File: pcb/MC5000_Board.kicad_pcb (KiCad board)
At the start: 2 copper layers, 100 x 97.5 mm, 44 parts, among them J1 USB_B_Micro, J10 Conn_01x04_Male, J11 Conn_01x04_Male, J12 Conn_01x04_Male, J13 Conn_01x04_Male, J2 Conn_01x04_Male, J3 Conn_01x04_Male, J4 Conn_01x04_Male, J5 Conn_01x04_Male, J6 Conn_01x04_Male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

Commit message: fixes
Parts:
- added C3: 0.1uF, Capacitor_SMD:C_0603_1608Metric_Pad1.08x0.95mm_HandSolder, F.Cu at (106.0, 46.5)
- added C4: 0.1uF, Capacitor_SMD:C_0603_1608Metric_Pad1.08x0.95mm_HandSolder, F.Cu at (110.5, 57.2)
- added D1: LED, LED_SMD:LED_0805_2012Metric_Pad1.15x1.40mm_HandSolder, F.Cu at (53.9, 54.8)
- added J14: Conn_01x04_Female, Connector_PinSocket_2.54mm:PinSocket_1x04_P2.54mm_Vertical, F.Cu at (106.7, 57.2)
- added J15: Conn_01x04_Female, Connector_PinSocket_2.54mm:PinSocket_1x04_P2.54mm_Vertical, F.Cu at (114.3, 64.8)
- added R10: 10k, Resistor_SMD:R_0603_1608Metric_Pad0.98x0.95mm_HandSolder, F.Cu at (110.5, 65.3)
- added R11: 10k, Resistor_SMD:R_0603_1608Metric_Pad0.98x0.95mm_HandSolder, F.Cu at (110.5, 62.6)
- added R12: 10k, Resistor_SMD:R_0603_1608Metric_Pad0.98x0.95mm_HandSolder, F.Cu at (110.5, 59.9)
- added R9: 200R, Resistor_SMD:R_0603_1608Metric_Pad0.98x0.95mm_HandSolder, F.Cu at (54.1, 44.4)
- moved U8 2.70 mm to (112.3, 48.5)
- moved DS1 2.48 mm to (76.1, 54.5)
- moved R1 2.48 mm to (100.2, 44.5)
- moved R2 2.48 mm to (100.2, 61.4)
- moved R3 2.48 mm to (100.2, 58.7)
- moved R4 2.48 mm to (100.2, 55.9)
- moved R5 2.48 mm to (100.2, 50.0)
- moved R6 2.48 mm to (100.2, 47.4)
- moved R7 2.48 mm to (100.2, 53.1)
- moved R8 2.48 mm to (100.2, 64.5)
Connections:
- U8 pad 12: Net-(U8-Pad12) -> GND
- U8 pad 2: Net-(U8-Pad2) -> GND
- U8 pad 21: Net-(U8-Pad21) -> GND
- U8 pad 24: Net-(U8-Pad24) -> VCC
- U8 pad 3: Net-(U8-Pad3) -> GND
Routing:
- net VCC: track 10.1 -> 146.4 mm, vias 2 -> 3
- net Net-(R9-Pad2): track 0.00 -> 70.4 mm
- net Net-(J15-Pad1): track 0.00 -> 29.7 mm
- net Net-(J15-Pad2): track 0.00 -> 26.9 mm
- net Net-(R8-Pad2): track 0.00 -> 22.8 mm
- net Net-(R2-Pad2): track 0.00 -> 19.7 mm
- net Net-(R5-Pad2): track 0.00 -> 19.0 mm
- net Net-(R1-Pad2): track 0.00 -> 18.0 mm
- net Net-(J15-Pad3): track 0.00 -> 17.8 mm, vias 0 -> 1
- net Net-(R3-Pad2): track 0.00 -> 16.7 mm
- net Net-(R4-Pad2): track 0.00 -> 14.8 mm
- net Net-(DS1-Pad8): track 25.3 -> 39.2 mm
- net Net-(DS1-Pad12): track 36.9 -> 50.8 mm
- net Net-(R6-Pad2): track 0.00 -> 13.4 mm
- net Net-(DS1-Pad7): track 21.0 -> 34.4 mm
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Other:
- board text added: "Buzzer IC"

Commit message: Work on PCB
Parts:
- added C5: 0.1uF, Capacitor_SMD:C_0603_1608Metric_Pad1.08x0.95mm_HandSolder, F.Cu at (61.5, 87.7)
- added C6: C, Capacitor_SMD:C_0603_1608Metric_Pad1.08x0.95mm_HandSolder, F.Cu at (69.3, 88.6)
- added C7: C, Capacitor_SMD:C_0603_1608Metric_Pad1.08x0.95mm_HandSolder, F.Cu at (69.3, 97.5)
- added J16: Conn_01x04_Female, Connector_PinSocket_2.54mm:PinSocket_1x04_P2.54mm_Vertical, F.Cu at (57.6, 87.8)
- added J17: Conn_01x04_Female, Connector_PinSocket_2.54mm:PinSocket_1x04_P2.54mm_Vertical, F.Cu at (57.9, 79.7)
- added J18: Conn_01x04_Female, Connector_PinSocket_2.54mm:PinSocket_1x04_P2.54mm_Vertical, F.Cu at (65.3, 95.4)
- added R13: 1M, Resistor_SMD:R_0603_1608Metric_Pad0.98x0.95mm_HandSolder, F.Cu at (61.5, 93.5)
- added R14: 1M, Resistor_SMD:R_0603_1608Metric_Pad0.98x0.95mm_HandSolder, F.Cu at (61.5, 90.6)
- added R15: 1M, Resistor_SMD:R_0603_1608Metric_Pad0.98x0.95mm_HandSolder, F.Cu at (69.3, 91.6)
- added R16: 1M, Resistor_SMD:R_0603_1608Metric_Pad0.98x0.95mm_HandSolder, F.Cu at (69.3, 94.5)
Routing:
- net Net-(J16-Pad3): track 0.00 -> 20.8 mm
- net Net-(C7-Pad2): track 0.00 -> 20.7 mm
- net Net-(J16-Pad2): track 0.00 -> 18.2 mm
- net TXD: track 10.6 -> 28.3 mm, vias 2 -> 1
- net Net-(C6-Pad2): track 0.00 -> 14.9 mm
- net VCC: track 146.4 -> 154.1 mm
- net RXD: track 14.4 -> 21.1 mm
- net Net-(J18-Pad2): track 0.00 -> 3.61 mm
- net Net-(J18-Pad1): track 0.00 -> 3.46 mm

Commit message: Nice labels
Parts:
- added ?: , buzzard_labels, F.Cu at (110.2, 66.5)
- added ?: , buzzard_labels, F.Cu at (61.9, 99.2)
- added ?: , buzzard_labels, F.Cu at (60.4, 105.5)
- added ?: , buzzard_labels, F.Cu at (65.7, 76.3)
- added ?: , buzzard_labels, F.Cu at (63.1, 76.5)
- added ?: , buzzard_labels, F.Cu at (60.5, 76.3)
- added ?: , buzzard_labels, F.Cu at (57.9, 76.5)
- added ?: , buzzard_labels, F.Cu at (61.8, 71.5)
- added ?: , buzzard_labels, F.Cu at (75.9, 67.1)
- added ?: , buzzard_labels, F.Cu at (140.0, 136.1)
- added ?: , buzzard_labels, F.Cu at (108.0, 136.1)
- added ?: , buzzard_labels, F.Cu at (124.0, 136.1)
- added ?: , buzzard_labels, F.Cu at (92.0, 136.1)
- added ?: , buzzard_labels, F.Cu at (75.8, 136.1)
- added ?: , buzzard_labels, F.Cu at (60.1, 136.1)
- R15, R16: value 1M -> 2K2
- moved C6 1.50 mm to (69.3, 87.1)
- moved C7 1.50 mm to (69.3, 96.0)
- moved R15 1.50 mm to (69.3, 90.1)
- moved R16 1.50 mm to (69.3, 93.0)
- moved J16 1.10 mm to (57.6, 88.9)
- moved R10 1.10 mm to (110.5, 64.2)
- moved R14 1.10 mm to (61.5, 91.7)
- moved C3 1.10 mm to (106.0, 45.4)
- moved C4 1.10 mm to (110.5, 56.1)
- moved DS1 1.10 mm to (76.1, 53.4)
- moved J14 1.10 mm to (106.7, 56.1)
- moved J15 1.10 mm to (114.3, 63.7)
- moved R1 1.10 mm to (100.2, 43.4)
- moved R11 1.10 mm to (110.5, 61.5)
- moved R12 1.10 mm to (110.5, 58.8)
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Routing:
- net Net-(J12-Pad1): track 16.9 -> 11.8 mm
- net Net-(C7-Pad2): track 20.7 -> 18.0 mm
- net Net-(C6-Pad2): track 14.9 -> 13.2 mm
- net Net-(J18-Pad2): track 3.61 -> 5.14 mm
- net Net-(J18-Pad1): track 3.46 -> 4.90 mm
- net VCC: track 154.1 -> 155.3 mm
- net RXD: track 21.1 -> 19.9 mm
- net TXD: track 28.3 -> 27.2 mm
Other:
- board text removed: "Buzzer IC"
- board text removed: "Display IC"
- board text removed: "MCU #1"
- board text removed: "MCU #2"
- board text removed: "MCU #3"

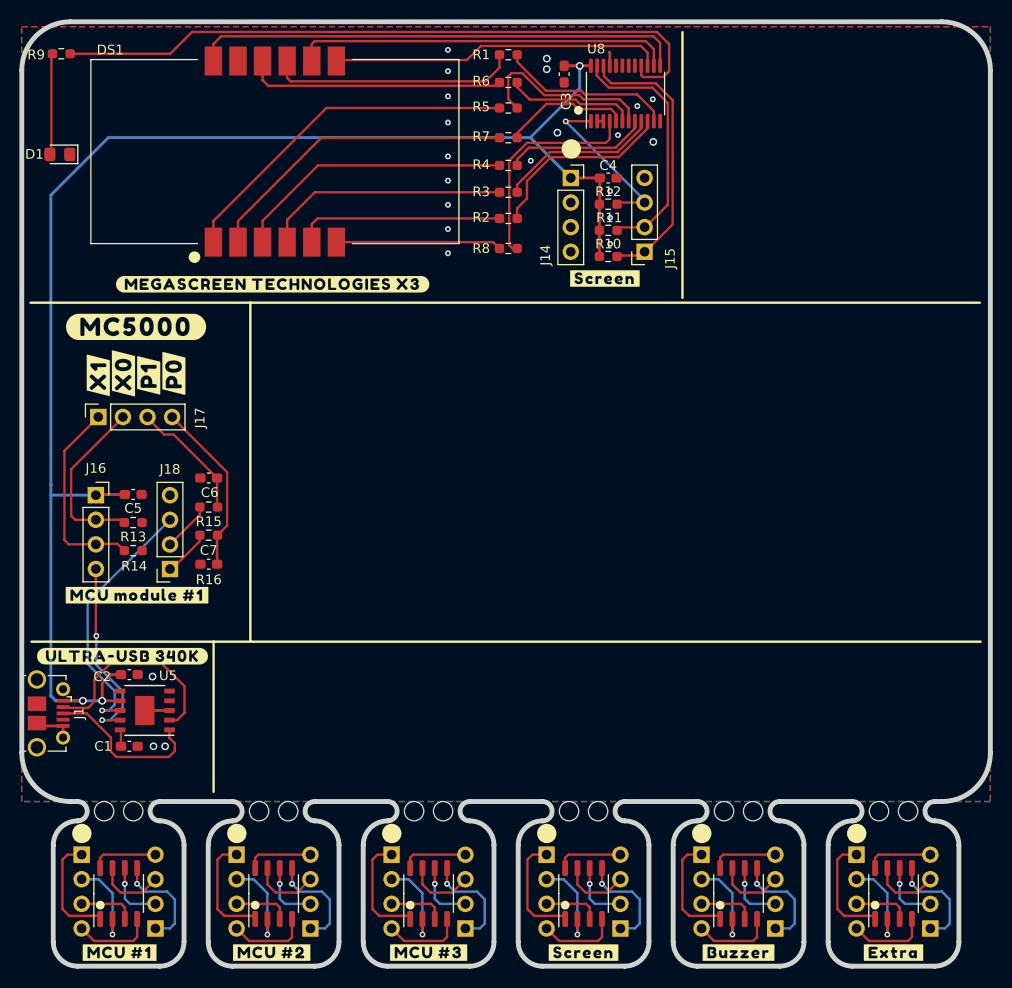
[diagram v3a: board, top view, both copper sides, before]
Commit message: Added buzzer
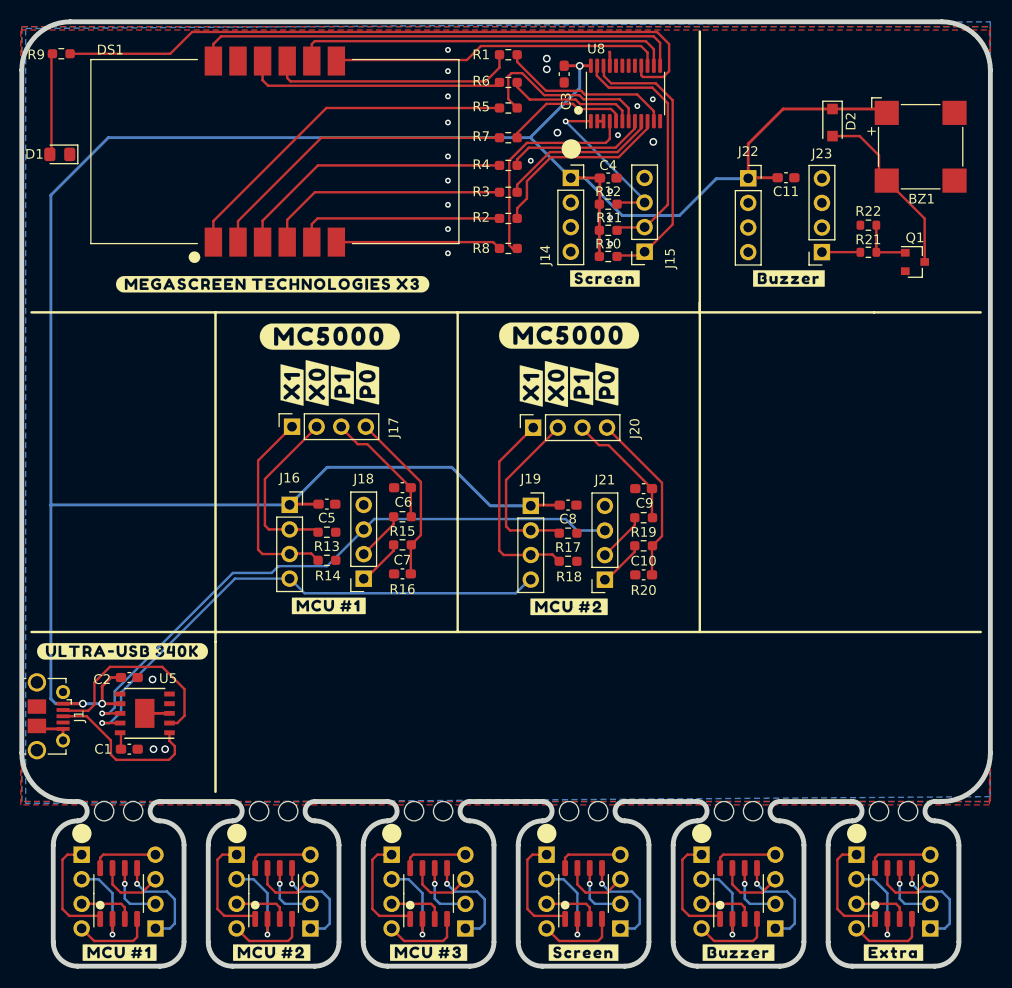
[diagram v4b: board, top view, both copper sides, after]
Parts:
- removed the ? at (61.9, 99.2)
- removed the ? at (65.7, 76.3)
- removed the ? at (63.1, 76.5)
- removed the ? at (60.5, 76.3)
- removed the ? at (57.9, 76.5)
- removed the ? at (61.8, 71.5)
- added ?: , buzzard_labels, F.Cu at (129.2, 66.5)
- added ?: , buzzard_labels, F.Cu at (81.8, 72.5)
- added ?: , buzzard_labels, F.Cu at (85.7, 77.3)
- added ?: , buzzard_labels, F.Cu at (106.5, 100.4)
- added ?: , buzzard_labels, F.Cu at (83.1, 77.5)
- added ?: , buzzard_labels, F.Cu at (80.5, 77.3)
- added ?: , buzzard_labels, F.Cu at (77.9, 77.5)
- added ?: , buzzard_labels, F.Cu at (81.7, 100.3)
- added ?: , buzzard_labels, F.Cu at (110.4, 77.4)
- added ?: , buzzard_labels, F.Cu at (105.2, 77.4)
- added ?: , buzzard_labels, F.Cu at (102.6, 77.6)
- added ?: , buzzard_labels, F.Cu at (107.8, 77.6)
- added ?: , buzzard_labels, F.Cu at (106.5, 72.4)
- added BZ1: MLT-7525, Buzzer_Beeper:MagneticBuzzer_CUI_CMT-8504-100-SMT, F.Cu at (142.8, 52.9)
- added C10: C, Capacitor_SMD:C_0603_1608Metric_Pad1.08x0.95mm_HandSolder, F.Cu at (114.2, 97.1)
- added C11: 0.1uF, Capacitor_SMD:C_0603_1608Metric_Pad1.08x0.95mm_HandSolder, F.Cu at (128.9, 56.1)
- added C8: 0.1uF, Capacitor_SMD:C_0603_1608Metric_Pad1.08x0.95mm_HandSolder, F.Cu at (106.4, 89.9)
- added C9: C, Capacitor_SMD:C_0603_1608Metric_Pad1.08x0.95mm_HandSolder, F.Cu at (114.2, 88.2)
- added D2: D, Diode_SMD:D_SOD-123F, F.Cu at (133.7, 50.4)
- added J19: Conn_01x04_Female, Connector_PinSocket_2.54mm:PinSocket_1x04_P2.54mm_Vertical, F.Cu at (102.5, 90.0)
- added J20: Conn_01x04_Female, Connector_PinSocket_2.54mm:PinSocket_1x04_P2.54mm_Vertical, F.Cu at (102.8, 81.9)
- added J21: Conn_01x04_Female, Connector_PinSocket_2.54mm:PinSocket_1x04_P2.54mm_Vertical, F.Cu at (110.2, 97.6)
- added J22: Conn_01x04_Female, Connector_PinSocket_2.54mm:PinSocket_1x04_P2.54mm_Vertical, F.Cu at (125.0, 56.2)
- added J23: Conn_01x04_Female, Connector_PinSocket_2.54mm:PinSocket_1x04_P2.54mm_Vertical, F.Cu at (132.6, 63.8)
- added Q1: S9013, Package_TO_SOT_SMD:SOT-23, F.Cu at (142.2, 64.8)
- added R17: 1M, Resistor_SMD:R_0603_1608Metric_Pad0.98x0.95mm_HandSolder, F.Cu at (106.4, 95.7)
- added R18: 1M, Resistor_SMD:R_0603_1608Metric_Pad0.98x0.95mm_HandSolder, F.Cu at (106.4, 92.8)
- added R19: 2K2, Resistor_SMD:R_0603_1608Metric_Pad0.98x0.95mm_HandSolder, F.Cu at (114.2, 91.2)
- added R20: 2K2, Resistor_SMD:R_0603_1608Metric_Pad0.98x0.95mm_HandSolder, F.Cu at (114.2, 94.1)
- added R21: 100R, Resistor_SMD:R_0603_1608Metric, F.Cu at (137.4, 63.8)
- added R22: 100k, Resistor_SMD:R_0603_1608Metric, F.Cu at (137.4, 61.0)
- moved J16 20.0 mm to (77.7, 89.9)
- moved J17 20.0 mm to (77.9, 81.8)
- moved C5 20.0 mm to (81.5, 89.8)
- moved C6 20.0 mm to (89.3, 88.1)
- moved C7 20.0 mm to (89.3, 97.0)
- moved J18 20.0 mm to (85.3, 97.5)
- moved R13 20.0 mm to (81.5, 95.6)
- moved R14 20.0 mm to (81.5, 92.7)
- moved R15 20.0 mm to (89.3, 91.1)
- moved R16 20.0 mm to (89.3, 94.0)
- moved ? 0.50 mm to (60.4, 105.0)
- moved U5 0.30 mm to (62.7, 111.4)
- moved C1 0.30 mm to (61.1, 115.1)
- moved C2 0.30 mm to (61.1, 107.7)
- moved J1 0.30 mm to (52.8, 111.7)
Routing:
- net VCC: track 155.3 -> 251.7 mm
- net TXD: track 27.2 -> 63.5 mm
- net RXD: track 19.9 -> 54.7 mm, vias 2 -> 1
- net Net-(J19-Pad3): track 0.00 -> 20.8 mm
- net Net-(BZ1-Pad2): track 0.00 -> 18.6 mm
- net Net-(J19-Pad2): track 0.00 -> 18.2 mm
- net Net-(C10-Pad2): track 0.00 -> 18.0 mm
- net Net-(C9-Pad2): track 0.00 -> 13.2 mm
- net Net-(Q1-Pad1): track 0.00 -> 5.81 mm
- net Net-(J21-Pad2): track 0.00 -> 5.14 mm
- net Net-(J21-Pad1): track 0.00 -> 4.90 mm
- net Net-(J23-Pad1): track 0.00 -> 3.97 mm

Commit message: Added LEDs
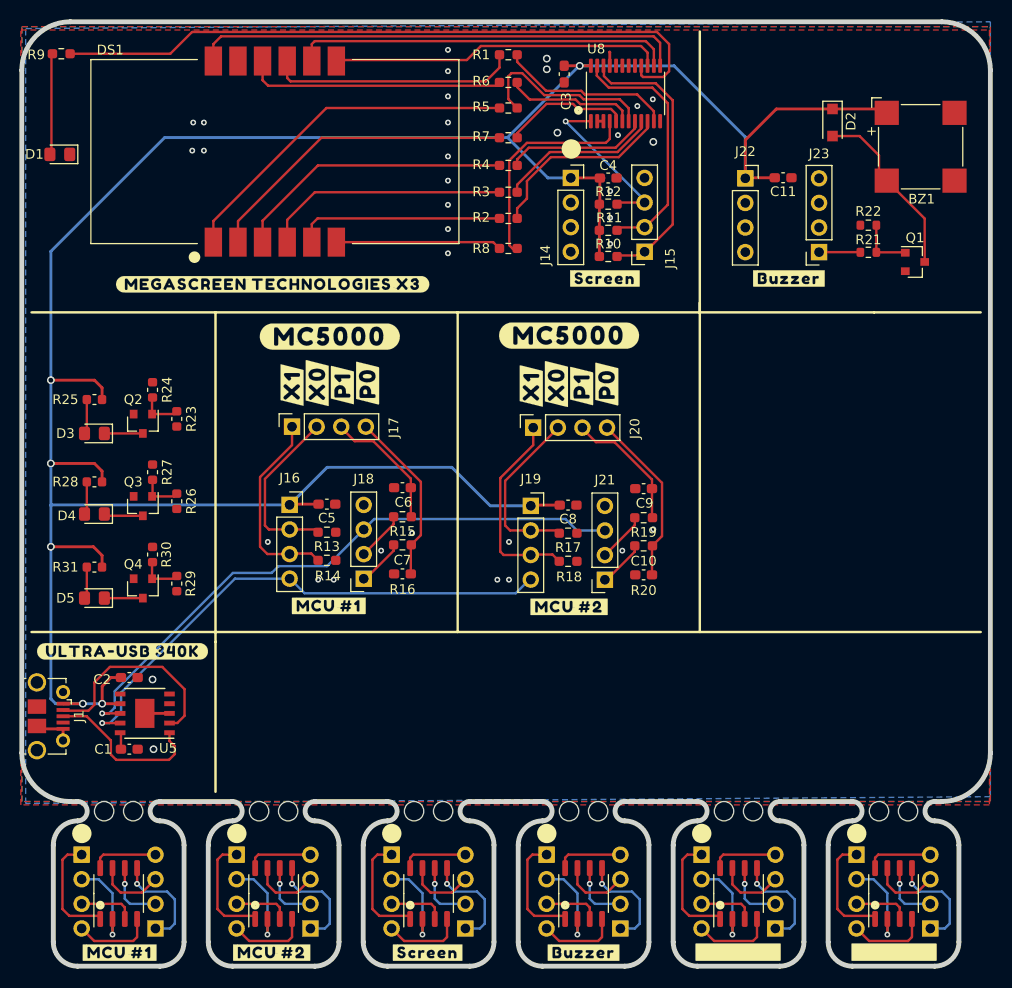
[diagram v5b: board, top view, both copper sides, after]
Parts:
- removed the ? at (140.0, 136.1)
- removed the ? at (92.0, 136.1)
- added D3: LED, LED_SMD:LED_0805_2012Metric_Pad1.15x1.40mm_HandSolder, F.Cu at (57.5, 82.5)
- added D4: LED, LED_SMD:LED_0805_2012Metric_Pad1.15x1.40mm_HandSolder, F.Cu at (57.5, 90.8)
- added D5: LED, LED_SMD:LED_0805_2012Metric_Pad1.15x1.40mm_HandSolder, F.Cu at (57.5, 99.5)
- added Q2: S9013, Package_TO_SOT_SMD:SOT-23, F.Cu at (62.5, 81.5)
- added Q3: S9013, Package_TO_SOT_SMD:SOT-23, F.Cu at (62.5, 90.0)
- added Q4: S9013, Package_TO_SOT_SMD:SOT-23, F.Cu at (62.5, 98.5)
- added R23: 100R, Resistor_SMD:R_0603_1608Metric, F.Cu at (66.0, 81.0)
- added R24: 100k, Resistor_SMD:R_0603_1608Metric, F.Cu at (63.5, 78.0)
- added R25: 150R, Resistor_SMD:R_0603_1608Metric, F.Cu at (57.5, 79.0)
- added R26: 100R, Resistor_SMD:R_0603_1608Metric, F.Cu at (66.0, 89.5)
- added R27: 100k, Resistor_SMD:R_0603_1608Metric, F.Cu at (63.5, 86.5)
- added R28: 150R, Resistor_SMD:R_0603_1608Metric, F.Cu at (57.5, 87.5)
- added R29: 100R, Resistor_SMD:R_0603_1608Metric, F.Cu at (66.0, 98.0)
- added R30: 100k, Resistor_SMD:R_0603_1608Metric, F.Cu at (63.5, 95.0)
- added R31: 150R, Resistor_SMD:R_0603_1608Metric, F.Cu at (57.5, 96.3)
- moved ? 16.1 mm to (91.9, 136.1)
- moved ? 16.0 mm to (108.0, 136.1)
- moved C11 0.30 mm to (128.6, 56.1)
- moved J23 0.30 mm to (132.3, 63.8)
- moved J22 0.30 mm to (124.7, 56.2)
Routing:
- net VCC: track 251.7 -> 273.3 mm, vias 3 -> 6
- net Net-(Q3-Pad1): track 0.00 -> 4.40 mm
- net Net-(Q4-Pad1): track 0.00 -> 4.40 mm
- net Net-(Q2-Pad1): track 0.00 -> 4.40 mm
- net Net-(D4-Pad1): track 0.00 -> 4.05 mm
- net Net-(D5-Pad1): track 0.00 -> 3.98 mm
- net Net-(D3-Pad1): track 0.00 -> 3.98 mm
- net Net-(D3-Pad2): track 0.00 -> 3.61 mm
- net Net-(D4-Pad2): track 0.00 -> 3.42 mm
- net Net-(D5-Pad2): track 0.00 -> 3.10 mm
- net Net-(C9-Pad2): track 13.2 -> 13.7 mm
- net Net-(C6-Pad2): track 13.2 -> 13.7 mm
- net GND: vias 23 -> 35

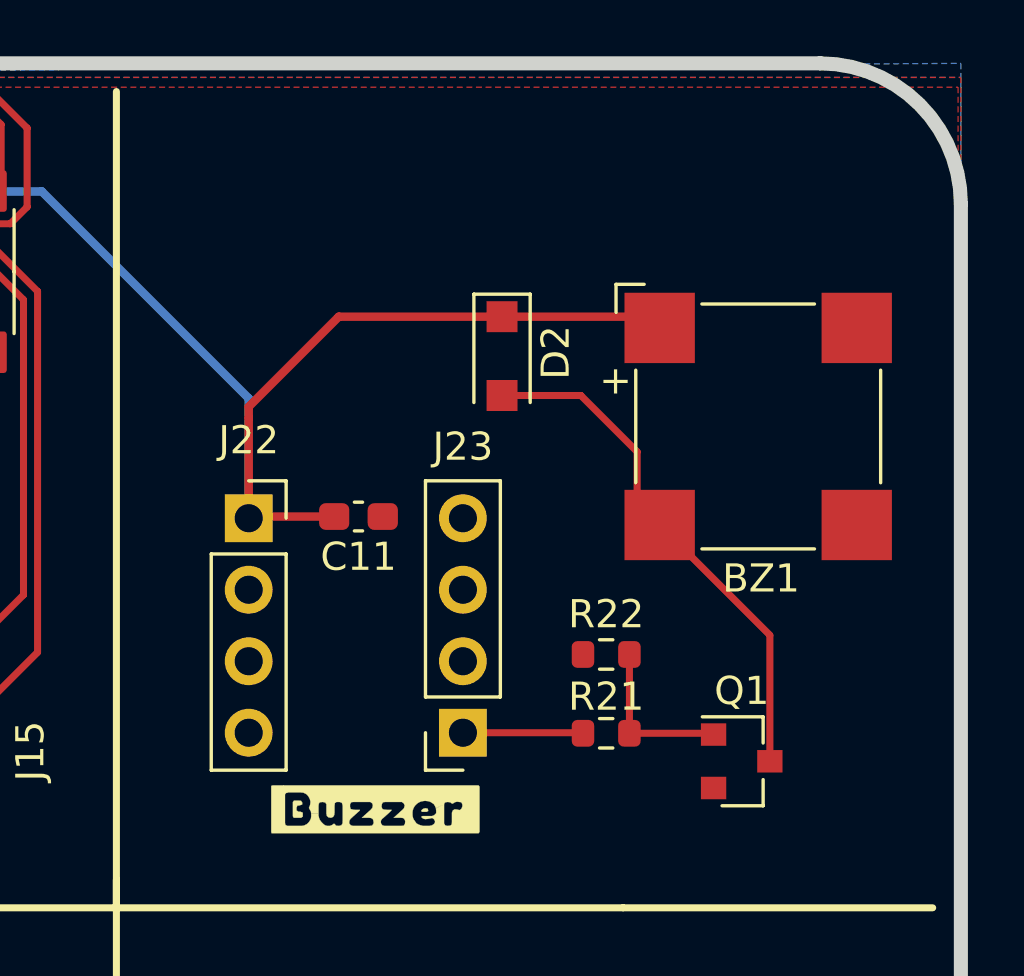
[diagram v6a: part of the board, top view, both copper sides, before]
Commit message: Added label for buzzer
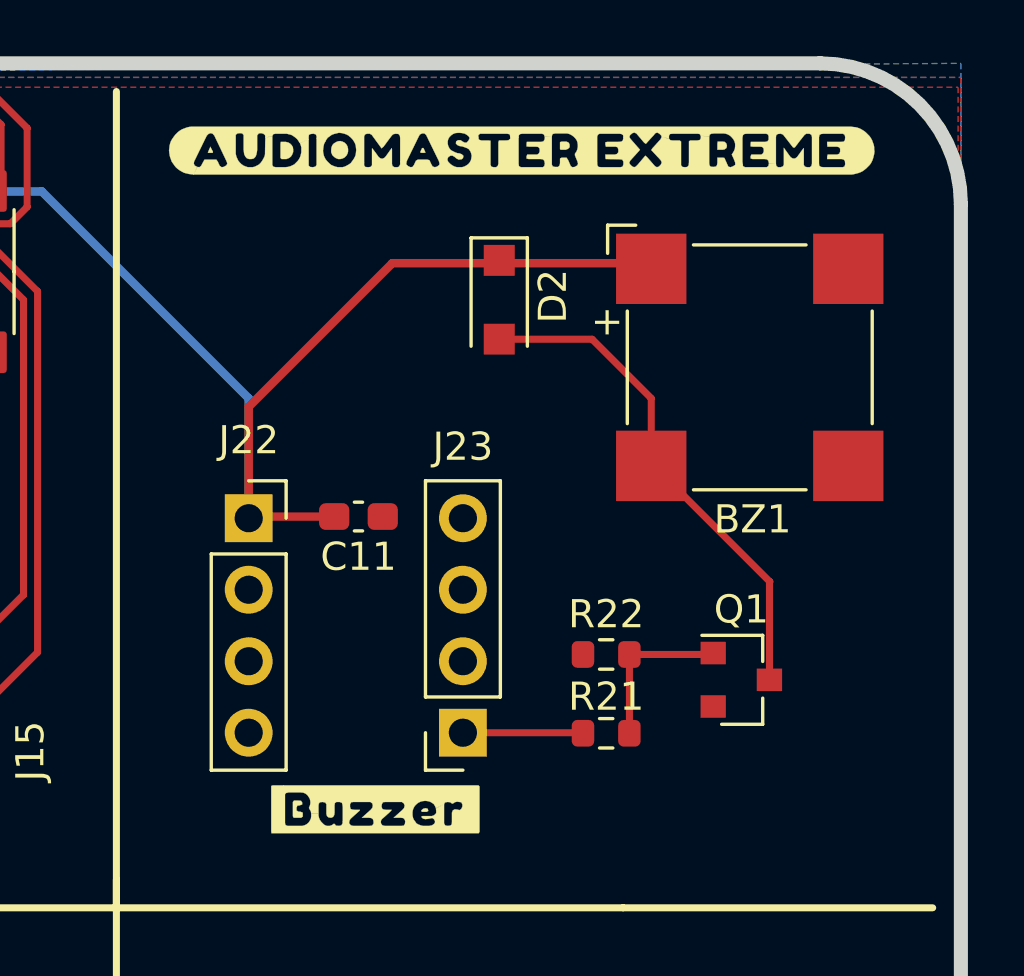
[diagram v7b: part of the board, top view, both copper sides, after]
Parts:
- added ?: , buzzard_labels, F.Cu at (134.4, 43.1)
- moved Q1 2.90 mm to (142.2, 61.9)
- moved BZ1 2.12 mm to (142.5, 50.8)
- moved D2 2.00 mm to (133.6, 48.4)

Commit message: Added switches
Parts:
- added ?: , buzzard_labels, F.Cu at (89.5, 105.0)
- added ?: , buzzard_labels, F.Cu at (60.3, 72.7)
- added R32: 100K, Resistor_SMD:R_0603_1608Metric_Pad0.98x0.95mm_HandSolder, F.Cu at (86.1, 114.5)
- added R33: 200R, Resistor_SMD:R_0603_1608Metric_Pad0.98x0.95mm_HandSolder, F.Cu at (86.1, 111.6)
- added R34: 100K, Resistor_SMD:R_0603_1608Metric_Pad0.98x0.95mm_HandSolder, F.Cu at (103.6, 114.5)
- added R35: 200R, Resistor_SMD:R_0603_1608Metric_Pad0.98x0.95mm_HandSolder, F.Cu at (103.6, 111.6)
- added SW1: SW_MEC_5E, Button_Switch_SMD:SW_Push_1P1T_NO_CK_KSC6xxJ, F.Cu at (78.9, 112.5)
- added SW2: SW_MEC_5E, Button_Switch_SMD:SW_Push_1P1T_NO_CK_KSC6xxJ, F.Cu at (96.6, 112.5)
- C10, C6, C7, C9: value C -> 0.1uF
- R10, R11: value 10k -> 2K2
- R12: value 10k -> 100K
- R21, R23, R26, R29: value 100R -> 200R
- R22, R24, R27, R30: value 100k -> 100K
- R25, R28, R31: value 150R -> 200R
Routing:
- net VCC: track 272.8 -> 320.1 mm, vias 6 -> 7
- net Net-(R32-Pad2): track 0.00 -> 12.1 mm
- net Net-(R34-Pad2): track 0.00 -> 11.9 mm
